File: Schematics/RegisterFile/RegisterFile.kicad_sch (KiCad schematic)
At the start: 4 parts, among them U1 74xx157, U2 7400, U3 74xx157, U4 74xx157

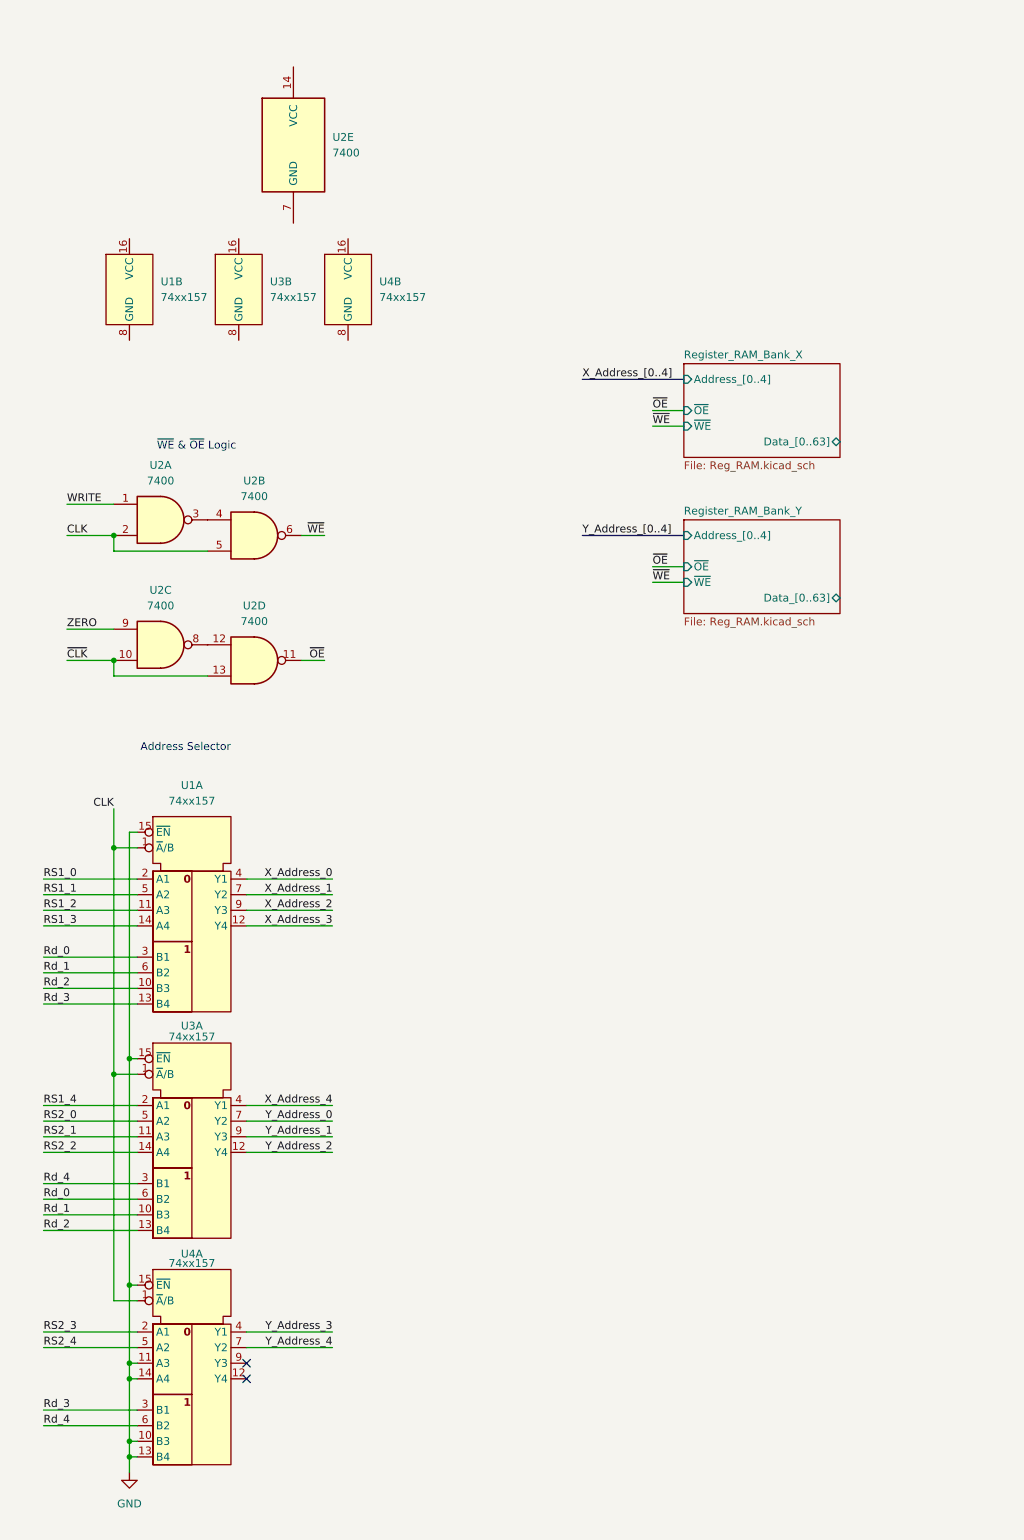
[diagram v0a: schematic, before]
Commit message: Updated RegFile diagrams + timing
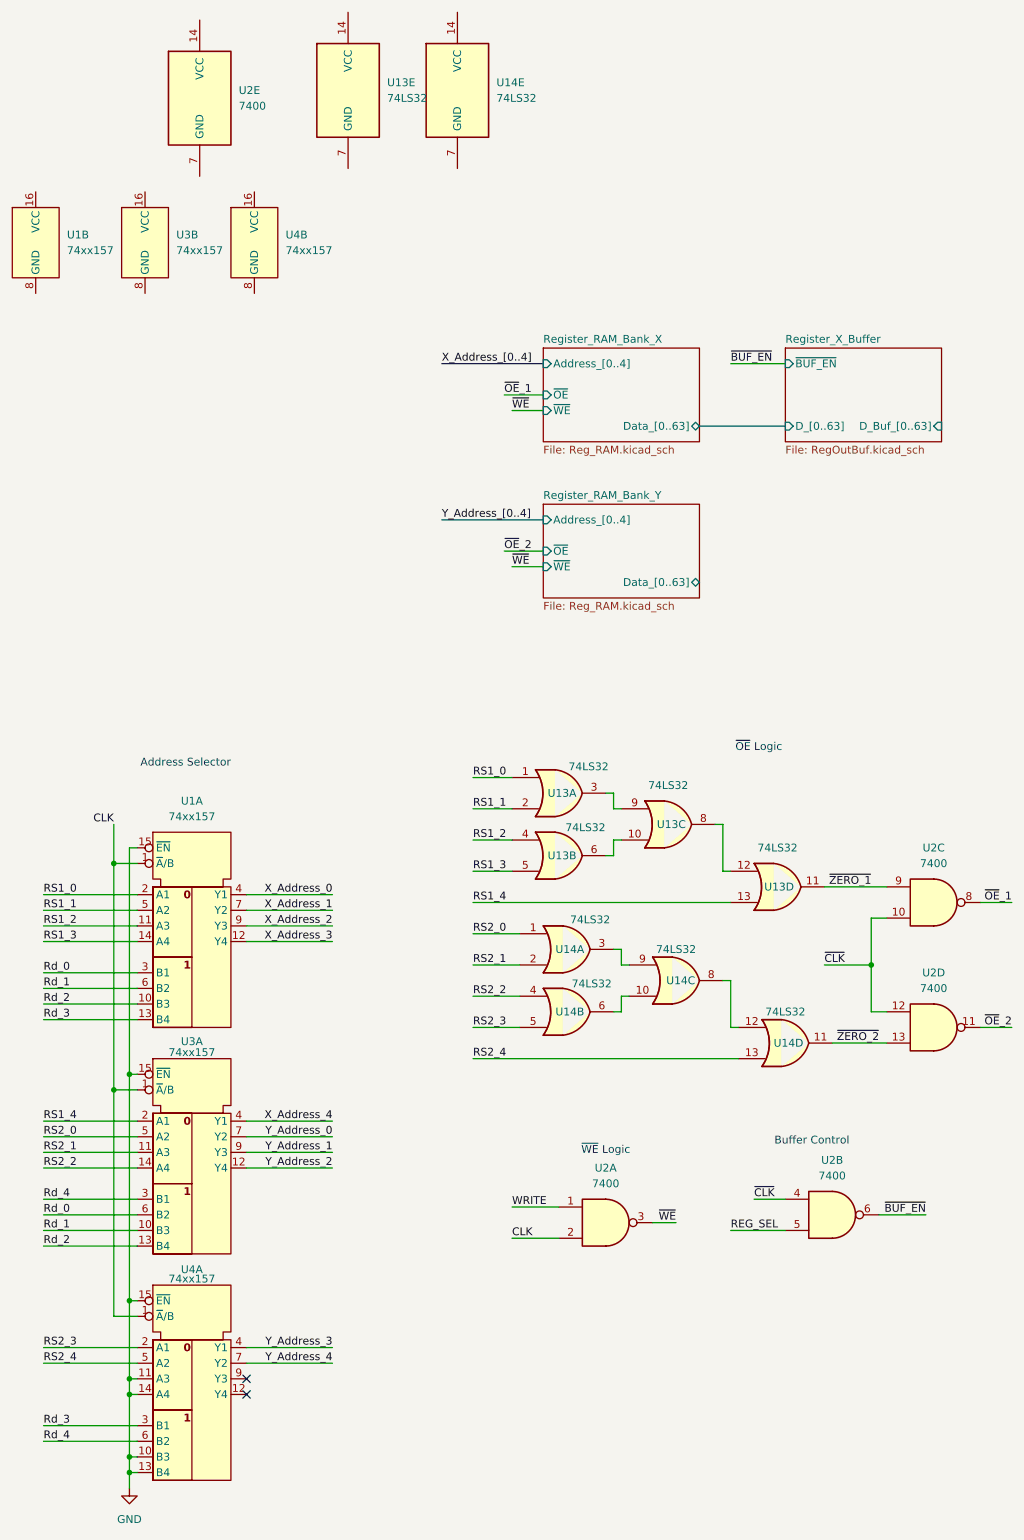
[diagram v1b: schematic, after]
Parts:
- added U13, U14: 74LS32, symbol 74xx:74LS32
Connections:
- net CLK: no longer U2.5
- net RS1_0: now also U13.1
- net RS1_1: now also U13.2
- net RS1_2: now also U13.4
- net RS1_3: now also U13.5
- net RS1_4: now also U13.13
- net RS2_0: now also U14.1
- net RS2_1: now also U14.2
- net RS2_2: now also U14.4
- net RS2_3: now also U14.5
- net RS2_4: now also U14.13
- net ~{CLK}: now also U2.12, U2.4; no longer U2.13
- net ~{WE}: now also U2.3; no longer U2.6
- net ~{OE}_1: now reaches U2.8
- net ~{OE}_1: no longer U2.12
- net ZERO renamed ~{ZERO_1}
- net ~{ZERO_1}: now also U13.11
- net ~{OE} renamed ~{OE}_2
- new net: U14.3, U14.9
- new net: U13.3, U13.9
- new net: U14.10, U14.6
- new net: U14.12, U14.8
- new net: U13.12, U13.8
- new net: U13.10, U13.6
- new net REG_SEL: U2.5
- new net ~{BUF_EN}: U2.6
- new net ~{ZERO_2}: U14.11, U2.13
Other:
- added sheet Register_X_Buffer (RegOutBuf.kicad_sch)
- note added: "Buffer Control"
- note added: "~{OE} Logic"
- note added: "~{WE} Logic"
- note removed: "~{WE} & ~{OE} Logic"
- moved on the sheet: U1A, U1B, U2A, U2E, U3A, U3B, U4A, U4B

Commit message: BIG UPDATE: Schematics, PCB & updated writeup for register
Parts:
- removed unit 4 of U13
- removed unit 3 of U13
- removed unit 2 of U13
- removed unit 3 of U14
- removed unit 4 of U14
- removed unit 2 of U14
- added C1, C10, C11, C3, C5, C7, C9: 0.1uF, Capacitor_SMD:C_1206_3216Metric, symbol Device:C
- added C2, C4, C6, C8: 10uF, Capacitor_SMD:C_1206_3216Metric, symbol Device:C
- added N1, N2: PCIE_16x, Connector_PCBEdge:BUS_PCIexpress_x16, symbol Connectors_Custom:PCIE_16x
- added unit 3 of U4
- added unit 2 of U4
- added unit 4 of U4
- added unit 3 of U5
- added unit 2 of U5
- added unit 4 of U5
- added unit 5 of U6
- added unit 1 of U7
- added unit 2 of U7
- added unit 4 of U7
- added unit 3 of U7
- U1: value 74xx157 -> 74157; footprint (none) -> Package_SO:SOIC-16_3.9x9.9mm_P1.27mm
- U2: renamed from U3; value 74xx157 -> 74157; footprint (none) -> Package_SO:SOIC-16_3.9x9.9mm_P1.27mm
- U3: renamed from U4; value 74xx157 -> 74157; footprint (none) -> Package_SO:SOIC-16_3.9x9.9mm_P1.27mm
- U4: renamed from U13; footprint (none) -> Package_SO:TSSOP-14_4.4x5mm_P0.65mm
- U5: renamed from U14; footprint (none) -> Package_SO:TSSOP-14_4.4x5mm_P0.65mm
- U6, U7: renamed from U2; footprint (none) -> Package_SO:TSSOP-14_4.4x5mm_P0.65mm
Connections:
- net WRITE is gone; now on net CLK: U6.1
- net CLK: now also N1.A2 (A01); no longer U6.2
- net GND: now also U1.8 (GND), U2.8 (GND), U3.2 (A1), U3.3 (B1), U3.5 (A2), U3.6 (B2), U3.8 (GND), U4.7 (GND), U5.7 (GND), U7.7 (GND), C1.2, C10.2, C11.2, C2.2, C3.2, C4.2, C5.2, C6.2, C7.2, C8.2, C9.2, N1.A11 (A10), N1.A12 (A11), N1.A17 (A16), N1.A22 (A21), N1.A27 (A26), N1.A3 (A02), N1.A31 (A30), N1.A32 (A31), N1.A33 (A32), N1.A34 (A33), N1.A35 (A34), N1.A36 (A35), N1.A37 (A36), N1.A38 (A37), N1.A39 (A38), N1.A40 (A39), N1.A41 (A40), N1.A43 (A42), N1.A44 (A43), N1.A45 (A44), N1.A46 (A45), N1.A47 (A46), N1.A48 (A47), N1.A49 (A48), N1.A5 (A04), N1.A50 (A49), N1.A51 (A50), N1.A52 (A51), N1.A53 (A52), N1.A54 (A53), N1.A55 (A54), N1.A56 (A55), N1.A57 (A56), N1.A58 (A57), N1.A59 (A58), N1.A60 (A59), N1.A61 (A60), N1.A62 (A61), N1.A63 (A62), N1.A64 (A63), N1.A65 (A64), N1.A66 (A65), N1.A67 (A66), N1.A68 (A67), N1.A69 (A68), N1.A7 (A06), N1.A70 (A69), N1.A71 (A70), N1.A72 (A71), N1.A73 (A72), N1.A74 (A73), N1.A75 (A74), N1.A76 (A75), N1.A77 (A76), N1.A78 (A77), N1.A79 (A78), N1.A80 (A79), N1.A81 (A80), N1.A82 (A81), N1.A9 (A08), N1.B11 (B10), N1.B16 (B15), N1.B21 (B20), N1.B26 (B25), N1.B31 (B30), N1.B36 (B35), N1.B41 (B40), N1.B47 (B46), N1.B52 (B51), N1.B57 (B56), N1.B6 (B05), N1.B62 (B61), N1.B67 (B66), N1.B72 (B71), N1.B77 (B76), N1.B82 (B81), N2.A11 (A10), N2.A16 (A15), N2.A21 (A20), N2.A26 (A25), N2.A31 (A30), N2.A36 (A35), N2.A42 (A41), N2.A47 (A46), N2.A52 (A51), N2.A57 (A56), N2.A6 (A05), N2.A62 (A61), N2.A67 (A66), N2.A72 (A71), N2.A77 (A76), N2.A82 (A81), N2.B11 (B10), N2.B16 (B15), N2.B21 (B20), N2.B26 (B25), N2.B31 (B30), N2.B36 (B35), N2.B42 (B41), N2.B47 (B46), N2.B52 (B51), N2.B57 (B56), N2.B6 (B05), N2.B62 (B61), N2.B67 (B66), N2.B72 (B71), N2.B77 (B76), N2.B82 (B81), U6.7 (GND), U7.10, U7.12, U7.13, U7.4, U7.5, U7.9; no longer U3.10 (B3), U3.11 (A3), U3.13 (B4), U3.14 (A4)
- net RS1_0: now also U1.11 (A3), N1.A13 (A12); no longer U1.2 (A1)
- net RS1_1: now also U1.14 (A4), N1.A14 (A13); no longer U1.5 (A2)
- net RS1_2: now also U1.2 (A1), N1.A15 (A14), U4.12; no longer U1.11 (A3)
- net RS1_3: now also U1.5 (A2), N1.A16 (A15), U4.13; no longer U1.14 (A4)
- net RS1_4: now also N1.A18 (A17), U4.10
- net RS2_0: now also U2.11 (A3), N1.A25 (A24); no longer U2.5 (A2)
- net RS2_1: now also U2.14 (A4), N1.A26 (A25); no longer U2.11 (A3)
- net RS2_2: now also U2.5 (A2), N1.A28 (A27), U5.13; no longer U2.14 (A4)
- net RS2_3: now also U3.11 (A3), N1.A29 (A28), U5.12; no longer U3.2 (A1)
- net RS2_4: now also U3.14 (A4), N1.A30 (A29), U5.10; no longer U3.5 (A2)
- net Rd_0: now also U1.10 (B3), U2.10 (B3), N1.A19 (A18); no longer U1.3 (B1), U2.6 (B2)
- net Rd_1: now also U1.13 (B4), U2.13 (B4), N1.A20 (A19); no longer U1.6 (B2), U2.10 (B3)
- net Rd_2: now also U1.3 (B1), U2.6 (B2), N1.A21 (A20); no longer U1.10 (B3), U2.13 (B4)
- net Rd_3: now also U1.6 (B2), U3.10 (B3), N1.A23 (A22); no longer U1.13 (B4), U3.3 (B1)
- net Rd_4: now also U3.13 (B4), N1.A24 (A23); no longer U3.6 (B2)
- net X_Address_0: now also U1.9 (Y3); no longer U1.4 (Y1)
- net X_Address_1: now also U1.12 (Y4); no longer U1.7 (Y2)
- net X_Address_2: now also U1.4 (Y1); no longer U1.9 (Y3)
- net X_Address_3: now also U1.7 (Y2); no longer U1.12 (Y4)
- net Y_Address_0: now also U2.9 (Y3); no longer U2.7 (Y2)
- net Y_Address_1: now also U2.12 (Y4); no longer U2.9 (Y3)
- net Y_Address_2: now also U2.7 (Y2); no longer U2.12 (Y4)
- net Y_Address_3: now also U3.9 (Y3); no longer U3.4 (Y1)
- net Y_Address_4: now also U3.12 (Y4); no longer U3.7 (Y2)
- net ~{CLK}: now also N1.A4 (A03), U7.2
- net ~{ZERO_1}: now also U4.8
- net ~{ZERO_2}: now also U5.8
- net at U5.3: now also U5.4
- net at U4.3: now also U4.4
- net VCC: now reaches U4.14 (VCC)
- net VCC: now also U1.16 (VCC), U2.16 (VCC), U3.16 (VCC), U5.14 (VCC), U7.14 (VCC), C1.1, C10.1, C11.1, C2.1, C3.1, C4.1, C5.1, C6.1, C7.1, C8.1, C9.1, N1.A1 (A00), N1.A42 (A41), N1.B1 (B00), N1.B42 (B41), N2.A1 (A00), N2.A41 (A40), N2.B1 (B00), N2.B41 (B40), U6.14 (VCC)
- net REG_SEL renamed REG_SEL_X
- net REG_SEL_X: now also N1.A8 (A07)
- net ~{BUF_EN} renamed ~{BUF_EN_X}
- new net: U4.6, U4.9
- new net: U4.11, U4.5
- new net: U5.6, U5.9
- new net: U5.11, U5.5
- new net REG_OUT_X_0: N2.A81 (A80)
- new net REG_OUT_X_1: N2.A80 (A79)
- new net REG_OUT_X_10: N2.A69 (A68)
- new net REG_OUT_X_11: N2.A68 (A67)
- new net REG_OUT_X_12: N2.A66 (A65)
- new net REG_OUT_X_13: N2.A65 (A64)
- new net REG_OUT_X_14: N2.A64 (A63)
- new net REG_OUT_X_15: N2.A63 (A62)
- new net REG_OUT_X_16: N2.A61 (A60)
- new net REG_OUT_X_17: N2.A60 (A59)
- new net REG_OUT_X_18: N2.A59 (A58)
- new net REG_OUT_X_19: N2.A58 (A57)
- new net REG_OUT_X_2: N2.A79 (A78)
- new net REG_OUT_X_20: N2.A56 (A55)
- new net REG_OUT_X_21: N2.A55 (A54)
- new net REG_OUT_X_22: N2.A54 (A53)
- new net REG_OUT_X_23: N2.A53 (A52)
- new net REG_OUT_X_24: N2.A51 (A50)
- new net REG_OUT_X_25: N2.A50 (A49)
- new net REG_OUT_X_26: N2.A49 (A48)
- new net REG_OUT_X_27: N2.A48 (A47)
- new net REG_OUT_X_28: N2.A46 (A45)
- new net REG_OUT_X_29: N2.A45 (A44)
- new net REG_OUT_X_3: N2.A78 (A77)
- new net REG_OUT_X_30: N2.A44 (A43)
- new net REG_OUT_X_31: N2.A43 (A42)
- new net REG_OUT_X_32: N2.A40 (A39)
- new net REG_OUT_X_33: N2.A39 (A38)
- new net REG_OUT_X_34: N2.A38 (A37)
- new net REG_OUT_X_35: N2.A37 (A36)
- new net REG_OUT_X_36: N2.A35 (A34)
- new net REG_OUT_X_37: N2.A34 (A33)
- new net REG_OUT_X_38: N2.A33 (A32)
- new net REG_OUT_X_39: N2.A32 (A31)
- new net REG_OUT_X_4: N2.A76 (A75)
- new net REG_OUT_X_40: N2.A30 (A29)
- new net REG_OUT_X_41: N2.A29 (A28)
- new net REG_OUT_X_42: N2.A28 (A27)
- new net REG_OUT_X_43: N2.A27 (A26)
- new net REG_OUT_X_44: N2.A25 (A24)
- new net REG_OUT_X_45: N2.A24 (A23)
- new net REG_OUT_X_46: N2.A23 (A22)
- new net REG_OUT_X_47: N2.A22 (A21)
- new net REG_OUT_X_48: N2.A20 (A19)
- new net REG_OUT_X_49: N2.A19 (A18)
- new net REG_OUT_X_5: N2.A75 (A74)
- new net REG_OUT_X_50: N2.A18 (A17)
- new net REG_OUT_X_51: N2.A17 (A16)
- new net REG_OUT_X_52: N2.A15 (A14)
- new net REG_OUT_X_53: N2.A14 (A13)
- new net REG_OUT_X_54: N2.A13 (A12)
- new net REG_OUT_X_55: N2.A12 (A11)
- new net REG_OUT_X_56: N2.A10 (A09)
- new net REG_OUT_X_57: N2.A9 (A08)
- new net REG_OUT_X_58: N2.A8 (A07)
- new net REG_OUT_X_59: N2.A7 (A06)
- new net REG_OUT_X_6: N2.A74 (A73)
- new net REG_OUT_X_60: N2.A5 (A04)
- new net REG_OUT_X_61: N2.A4 (A03)
- new net REG_OUT_X_62: N2.A3 (A02)
- new net REG_OUT_X_63: N2.A2 (A01)
- new net REG_OUT_X_7: N2.A73 (A72)
- new net REG_OUT_X_8: N2.A71 (A70)
- new net REG_OUT_X_9: N2.A70 (A69)
- new net REG_OUT_Y_0: N2.B81 (B80)
- new net REG_OUT_Y_1: N2.B80 (B79)
- new net REG_OUT_Y_10: N2.B69 (B68)
- new net REG_OUT_Y_11: N2.B68 (B67)
- new net REG_OUT_Y_12: N2.B66 (B65)
- new net REG_OUT_Y_13: N2.B65 (B64)
- new net REG_OUT_Y_14: N2.B64 (B63)
- new net REG_OUT_Y_15: N2.B63 (B62)
- new net REG_OUT_Y_16: N2.B61 (B60)
- new net REG_OUT_Y_17: N2.B60 (B59)
- new net REG_OUT_Y_18: N2.B59 (B58)
- new net REG_OUT_Y_19: N2.B58 (B57)
- new net REG_OUT_Y_2: N2.B79 (B78)
- new net REG_OUT_Y_20: N2.B56 (B55)
- new net REG_OUT_Y_21: N2.B55 (B54)
- new net REG_OUT_Y_22: N2.B54 (B53)
- new net REG_OUT_Y_23: N2.B53 (B52)
- new net REG_OUT_Y_24: N2.B51 (B50)
- new net REG_OUT_Y_25: N2.B50 (B49)
- new net REG_OUT_Y_26: N2.B49 (B48)
- new net REG_OUT_Y_27: N2.B48 (B47)
- new net REG_OUT_Y_28: N2.B46 (B45)
- new net REG_OUT_Y_29: N2.B45 (B44)
- new net REG_OUT_Y_3: N2.B78 (B77)
- new net REG_OUT_Y_30: N2.B44 (B43)
- new net REG_OUT_Y_31: N2.B43 (B42)
- new net REG_OUT_Y_32: N2.B40 (B39)
- new net REG_OUT_Y_33: N2.B39 (B38)
- new net REG_OUT_Y_34: N2.B38 (B37)
- new net REG_OUT_Y_35: N2.B37 (B36)
- new net REG_OUT_Y_36: N2.B35 (B34)
- new net REG_OUT_Y_37: N2.B34 (B33)
- new net REG_OUT_Y_38: N2.B33 (B32)
- new net REG_OUT_Y_39: N2.B32 (B31)
- new net REG_OUT_Y_4: N2.B76 (B75)
- new net REG_OUT_Y_40: N2.B30 (B29)
- new net REG_OUT_Y_41: N2.B29 (B28)
- new net REG_OUT_Y_42: N2.B28 (B27)
- new net REG_OUT_Y_43: N2.B27 (B26)
- new net REG_OUT_Y_44: N2.B25 (B24)
- new net REG_OUT_Y_45: N2.B24 (B23)
- new net REG_OUT_Y_46: N2.B23 (B22)
- new net REG_OUT_Y_47: N2.B22 (B21)
- new net REG_OUT_Y_48: N2.B20 (B19)
- new net REG_OUT_Y_49: N2.B19 (B18)
- new net REG_OUT_Y_5: N2.B75 (B74)
- new net REG_OUT_Y_50: N2.B18 (B17)
- new net REG_OUT_Y_51: N2.B17 (B16)
- new net REG_OUT_Y_52: N2.B15 (B14)
- new net REG_OUT_Y_53: N2.B14 (B13)
- new net REG_OUT_Y_54: N2.B13 (B12)
- new net REG_OUT_Y_55: N2.B12 (B11)
- new net REG_OUT_Y_56: N2.B10 (B09)
- new net REG_OUT_Y_57: N2.B9 (B08)
- new net REG_OUT_Y_58: N2.B8 (B07)
- new net REG_OUT_Y_59: N2.B7 (B06)
- new net REG_OUT_Y_6: N2.B74 (B73)
- new net REG_OUT_Y_60: N2.B5 (B04)
- new net REG_OUT_Y_61: N2.B4 (B03)
- new net REG_OUT_Y_62: N2.B3 (B02)
- new net REG_OUT_Y_63: N2.B2 (B01)
- new net REG_OUT_Y_7: N2.B73 (B72)
- new net REG_OUT_Y_8: N2.B71 (B70)
- new net REG_OUT_Y_9: N2.B70 (B69)
- new net REG_SEL_Y: N1.A10 (A09), U7.1
- new net WB_DATA_0: N1.B2 (B01)
- new net WB_DATA_1: N1.B3 (B02)
- new net WB_DATA_10: N1.B14 (B13)
- new net WB_DATA_11: N1.B15 (B14)
- new net WB_DATA_12: N1.B17 (B16)
- new net WB_DATA_13: N1.B18 (B17)
- new net WB_DATA_14: N1.B19 (B18)
- new net WB_DATA_15: N1.B20 (B19)
- new net WB_DATA_16: N1.B22 (B21)
- new net WB_DATA_17: N1.B23 (B22)
- new net WB_DATA_18: N1.B24 (B23)
- new net WB_DATA_19: N1.B25 (B24)
- new net WB_DATA_2: N1.B4 (B03)
- new net WB_DATA_20: N1.B27 (B26)
- new net WB_DATA_21: N1.B28 (B27)
- new net WB_DATA_22: N1.B29 (B28)
- new net WB_DATA_23: N1.B30 (B29)
- new net WB_DATA_24: N1.B32 (B31)
- new net WB_DATA_25: N1.B33 (B32)
- new net WB_DATA_26: N1.B34 (B33)
- new net WB_DATA_27: N1.B35 (B34)
- new net WB_DATA_28: N1.B37 (B36)
- new net WB_DATA_29: N1.B38 (B37)
- new net WB_DATA_3: N1.B5 (B04)
- new net WB_DATA_30: N1.B39 (B38)
- new net WB_DATA_31: N1.B40 (B39)
- new net WB_DATA_32: N1.B43 (B42)
- new net WB_DATA_33: N1.B44 (B43)
- new net WB_DATA_34: N1.B45 (B44)
- new net WB_DATA_35: N1.B46 (B45)
- new net WB_DATA_36: N1.B48 (B47)
- new net WB_DATA_37: N1.B49 (B48)
- new net WB_DATA_38: N1.B50 (B49)
- new net WB_DATA_39: N1.B51 (B50)
- new net WB_DATA_4: N1.B7 (B06)
- new net WB_DATA_40: N1.B53 (B52)
- new net WB_DATA_41: N1.B54 (B53)
- new net WB_DATA_42: N1.B55 (B54)
- new net WB_DATA_43: N1.B56 (B55)
- new net WB_DATA_44: N1.B58 (B57)
- new net WB_DATA_45: N1.B59 (B58)
- new net WB_DATA_46: N1.B60 (B59)
- new net WB_DATA_47: N1.B61 (B60)
- new net WB_DATA_48: N1.B63 (B62)
- new net WB_DATA_49: N1.B64 (B63)
- new net WB_DATA_5: N1.B8 (B07)
- new net WB_DATA_50: N1.B65 (B64)
- new net WB_DATA_51: N1.B66 (B65)
- new net WB_DATA_52: N1.B68 (B67)
- new net WB_DATA_53: N1.B69 (B68)
- new net WB_DATA_54: N1.B70 (B69)
- new net WB_DATA_55: N1.B71 (B70)
- new net WB_DATA_56: N1.B73 (B72)
- new net WB_DATA_57: N1.B74 (B73)
- new net WB_DATA_58: N1.B75 (B74)
- new net WB_DATA_59: N1.B76 (B75)
- new net WB_DATA_6: N1.B9 (B08)
- new net WB_DATA_60: N1.B78 (B77)
- new net WB_DATA_61: N1.B79 (B78)
- new net WB_DATA_62: N1.B80 (B79)
- new net WB_DATA_63: N1.B81 (B80)
- new net WB_DATA_7: N1.B10 (B09)
- new net WB_DATA_8: N1.B12 (B11)
- new net WB_DATA_9: N1.B13 (B12)
- new net WRT: N1.A6 (A05), U6.2
- new net ~{BUF_EN_Y}: U7.3
- no-connect marks 2 -> 5
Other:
- removed sheet Register_RAM_Bank_X
- added sheet Register_RAM_Bank X (Reg_RAM_Inv.kicad_sch)
- added sheet Register_Y_Buffer (RegOutBuf.kicad_sch)
- added sheet WB_Buffer_X (Inv_Buffer.kicad_sch)
- added sheet WB_Buffer_Y (RegOutBuf.kicad_sch)
- sheet Register_X_Buffer: file RegOutBuf.kicad_sch -> Inv_Buffer.kicad_sch
- sheet Register_X_Buffer ports: added D_BUF_[0..63]; removed D_Buf_[0..63]
- note added: "Decoupling Capacitors"
- note added: "Inputs"
- note added: "Outputs"
- note added: "Power Connections"
- note added: "RAM ~{OE} Logic"
- note added: "REG_OUT_X"
- note added: "REG_OUT_Y"
- note added: "Unused Gates"
- note added: "WB_DATA"
- note added: "X/Y Buffer Control"
- note added: "X_BUS_[0..63]"
- note added: "Y_BUS_[0..63]"
- note removed: "Buffer Control"
- note removed: "~{OE} Logic"
- title: (none) -> THORN-2 Register Card
- moved on the sheet: U1A, U1B, U2A, U2B, U3A, U3B, U4A, U4E, U5A, U5E, U6A, U6B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
